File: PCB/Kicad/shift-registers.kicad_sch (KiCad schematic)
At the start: 7 parts

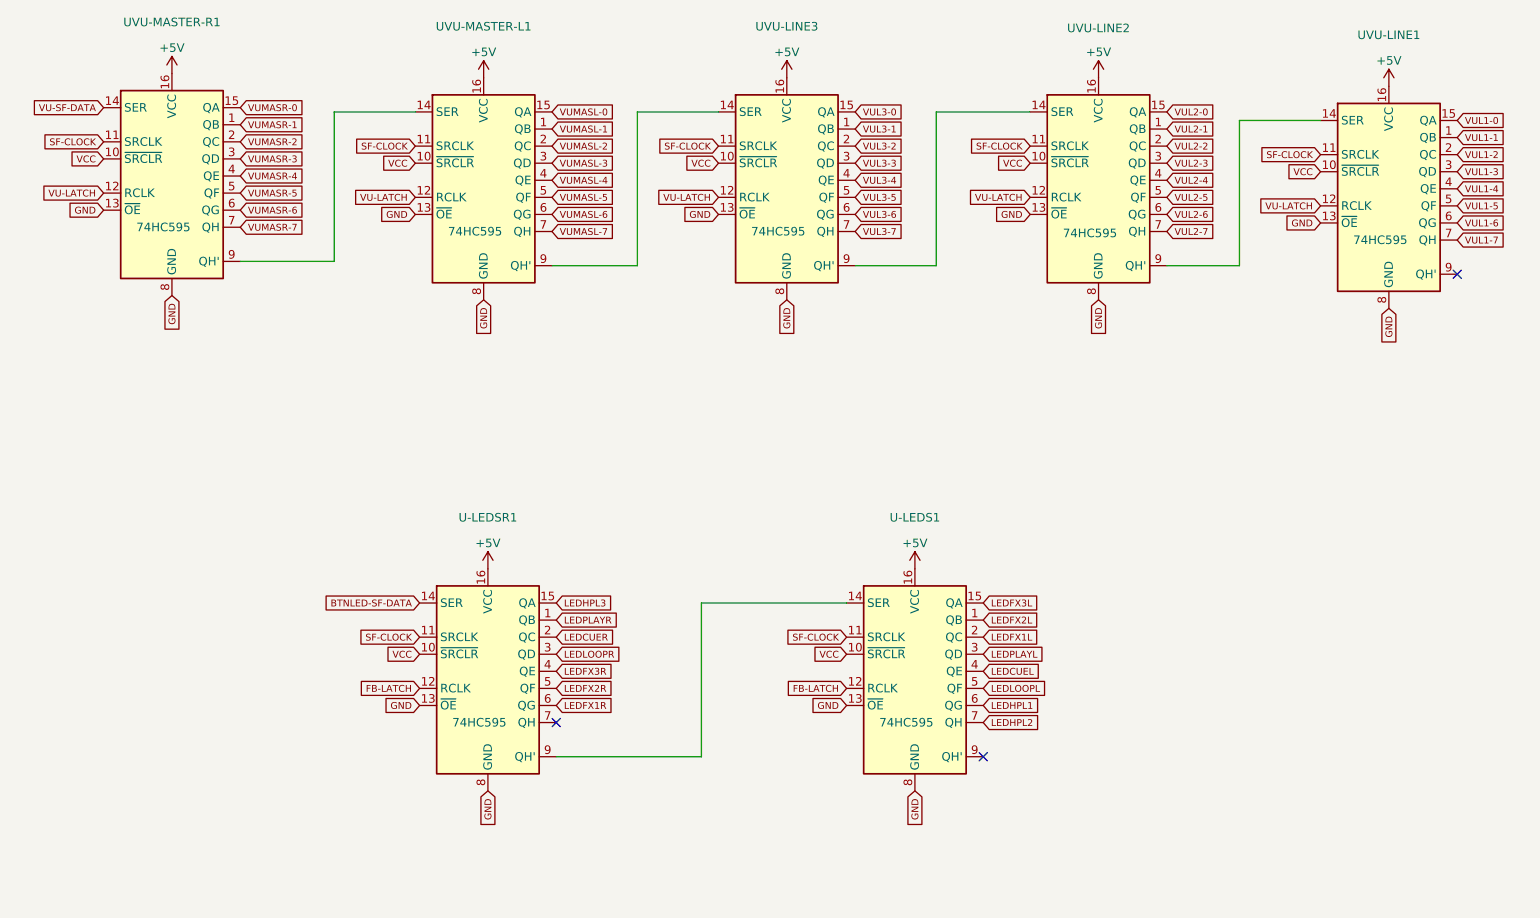
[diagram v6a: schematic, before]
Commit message: all neopixels together
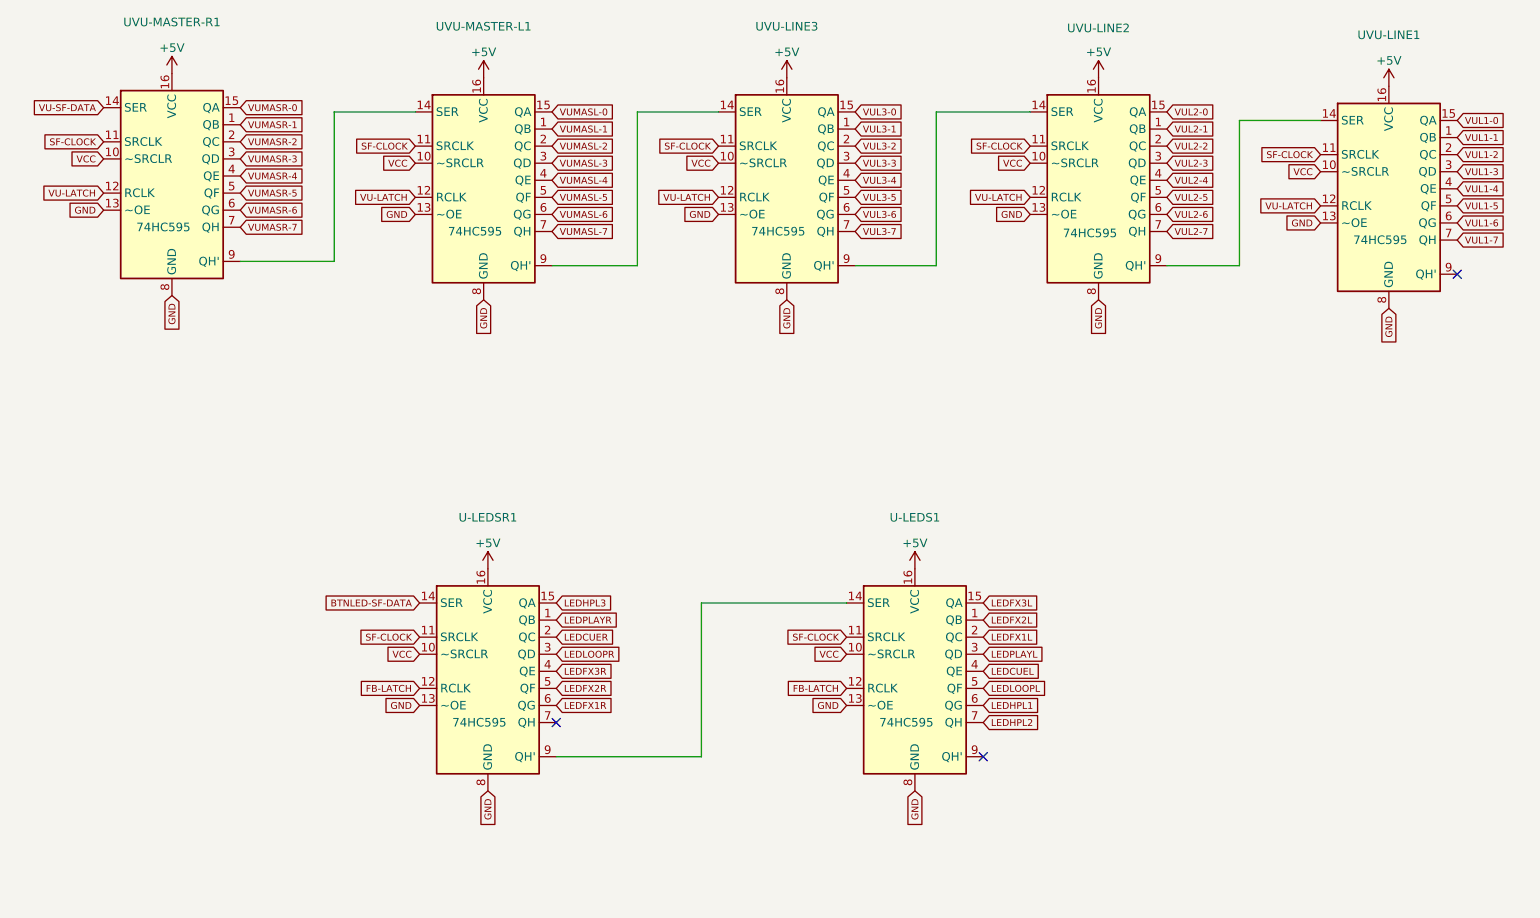
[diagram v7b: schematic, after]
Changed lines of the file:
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@@
-(kicad_sch (version 20210406) (generator eeschema)
+(kicad_sch (version 20210615) (generator eeschema)
   (paper "A4")
   (no_connect (at 109.22 130.81))

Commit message: changed encoders pins to interrupt pins
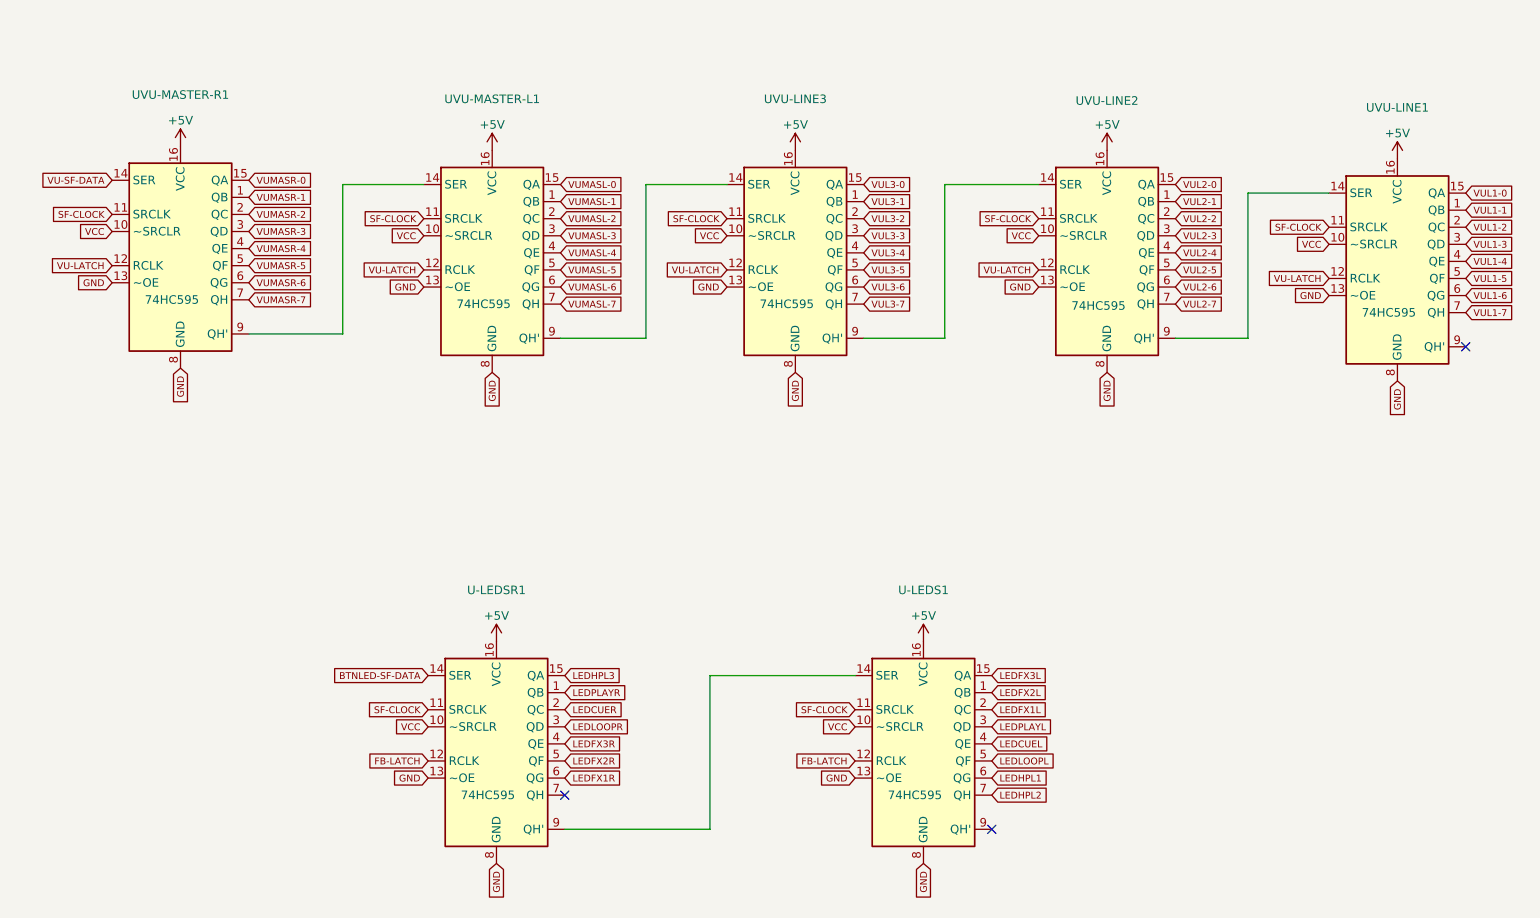
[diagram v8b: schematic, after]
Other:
- moved on the sheet: U-LEDS1, U-LEDSR1, UVU-LINE1, UVU-LINE2, UVU-LINE3, UVU-MASTER-L1, UVU-MASTER-R1
